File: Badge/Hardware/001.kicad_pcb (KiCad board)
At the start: 2 copper layers, 92.2 x 84.2 mm, 1 part

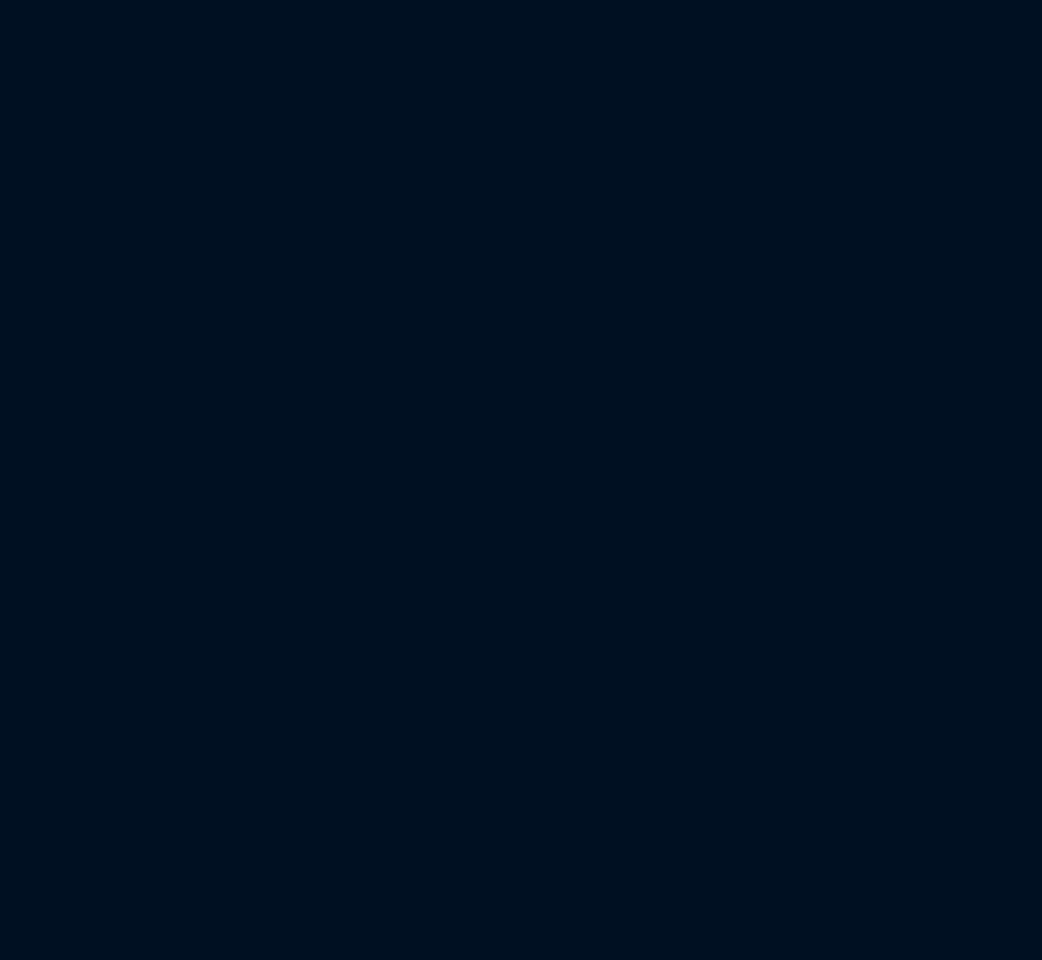
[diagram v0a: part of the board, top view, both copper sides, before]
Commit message: Add custom forms at SVG
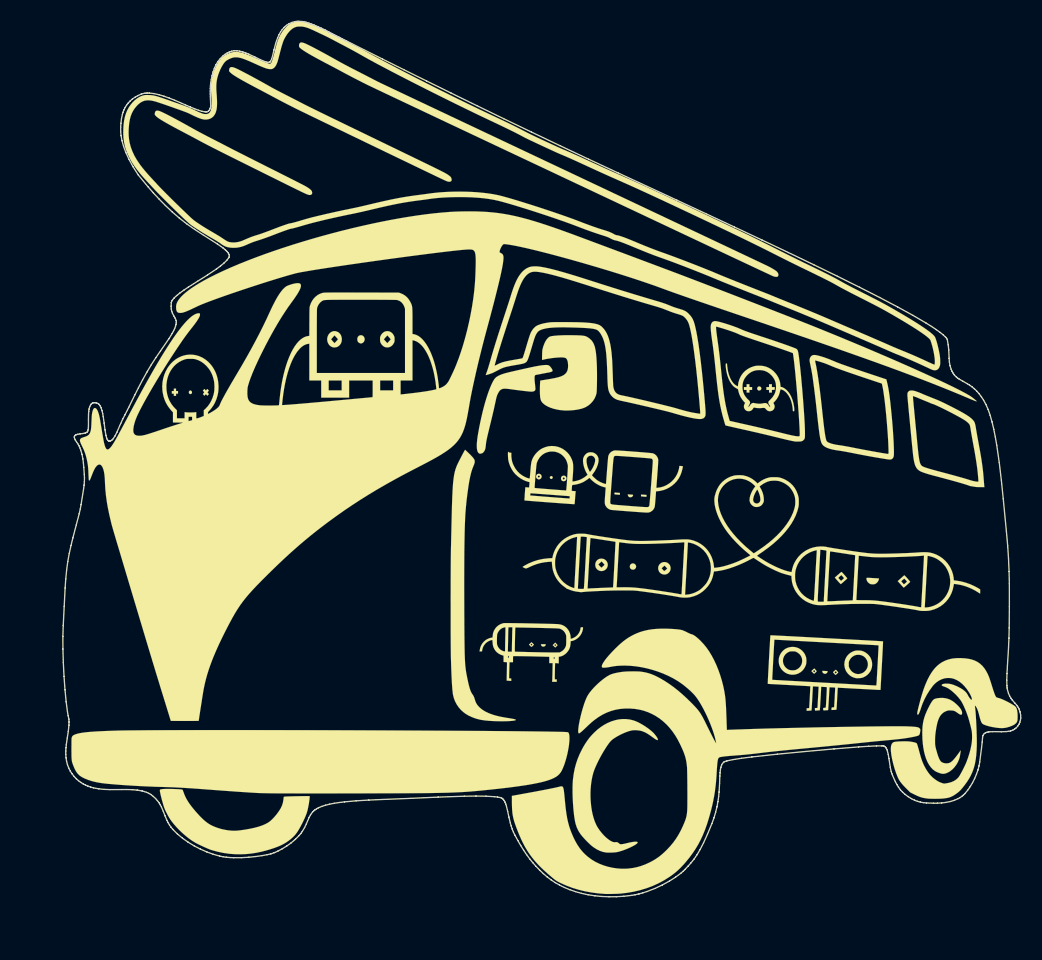
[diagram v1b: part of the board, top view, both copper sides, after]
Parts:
- added Ref**: Val**, combi:Combi_All_04, F.Cu at (232.4, 91.4)
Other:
- board size 92.2 x 84.2 mm -> 92.2 x 84.3 mm

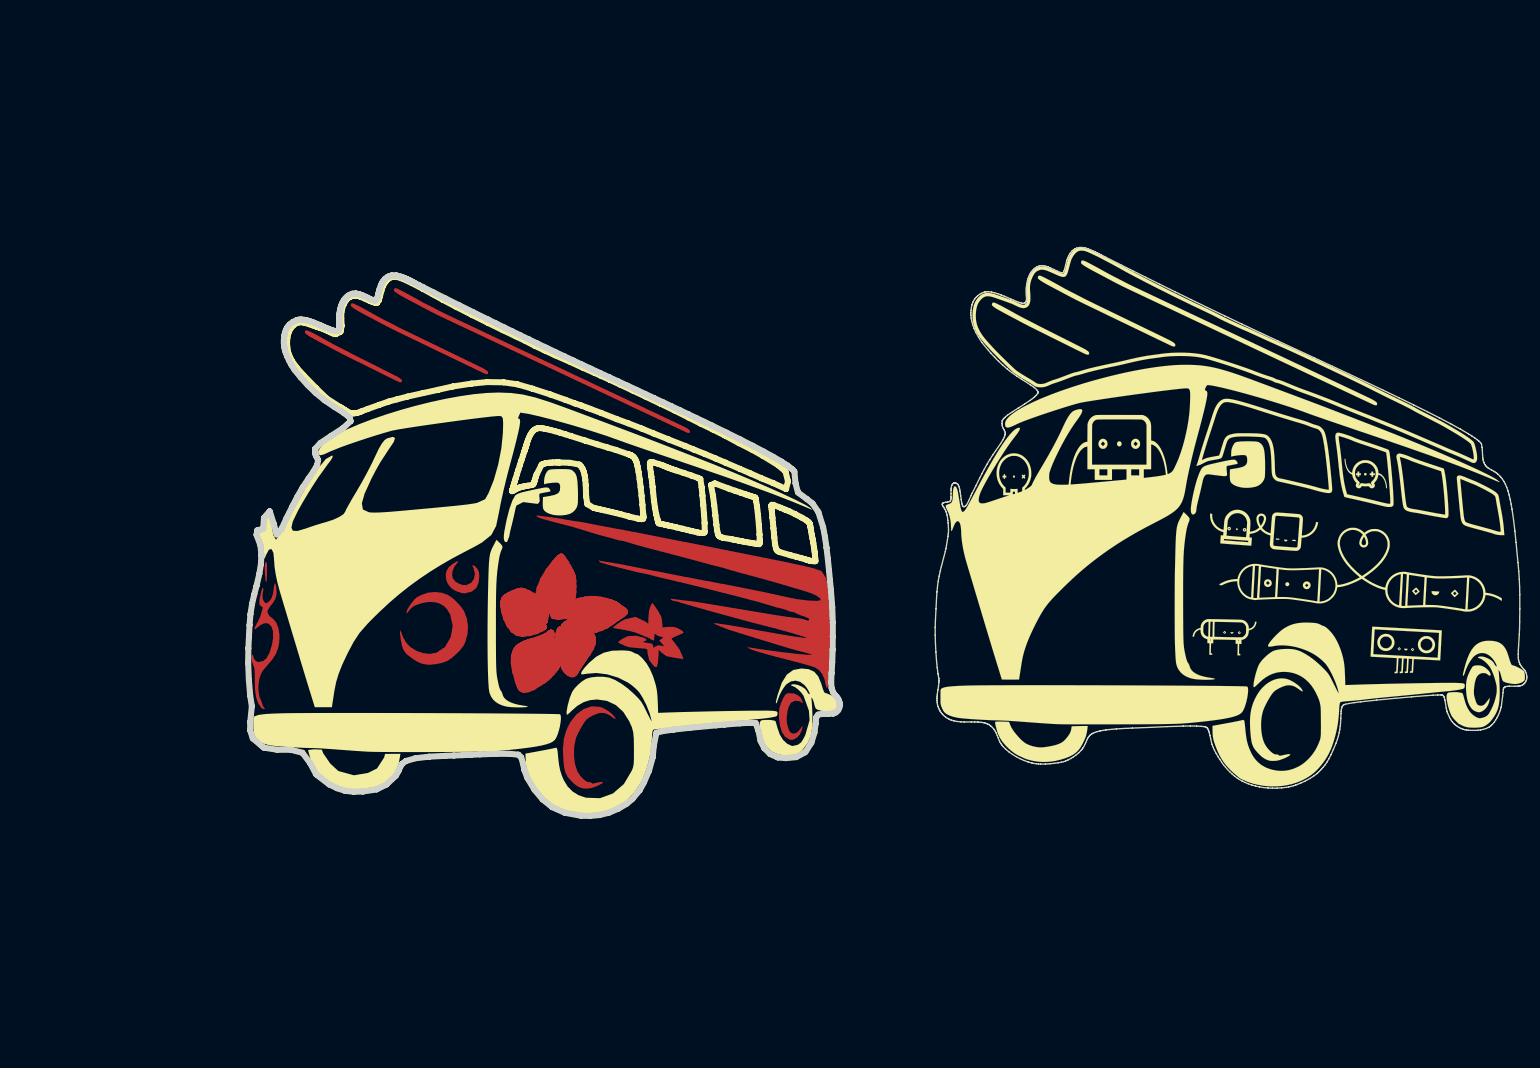
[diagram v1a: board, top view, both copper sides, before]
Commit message: Add custom art to SVG
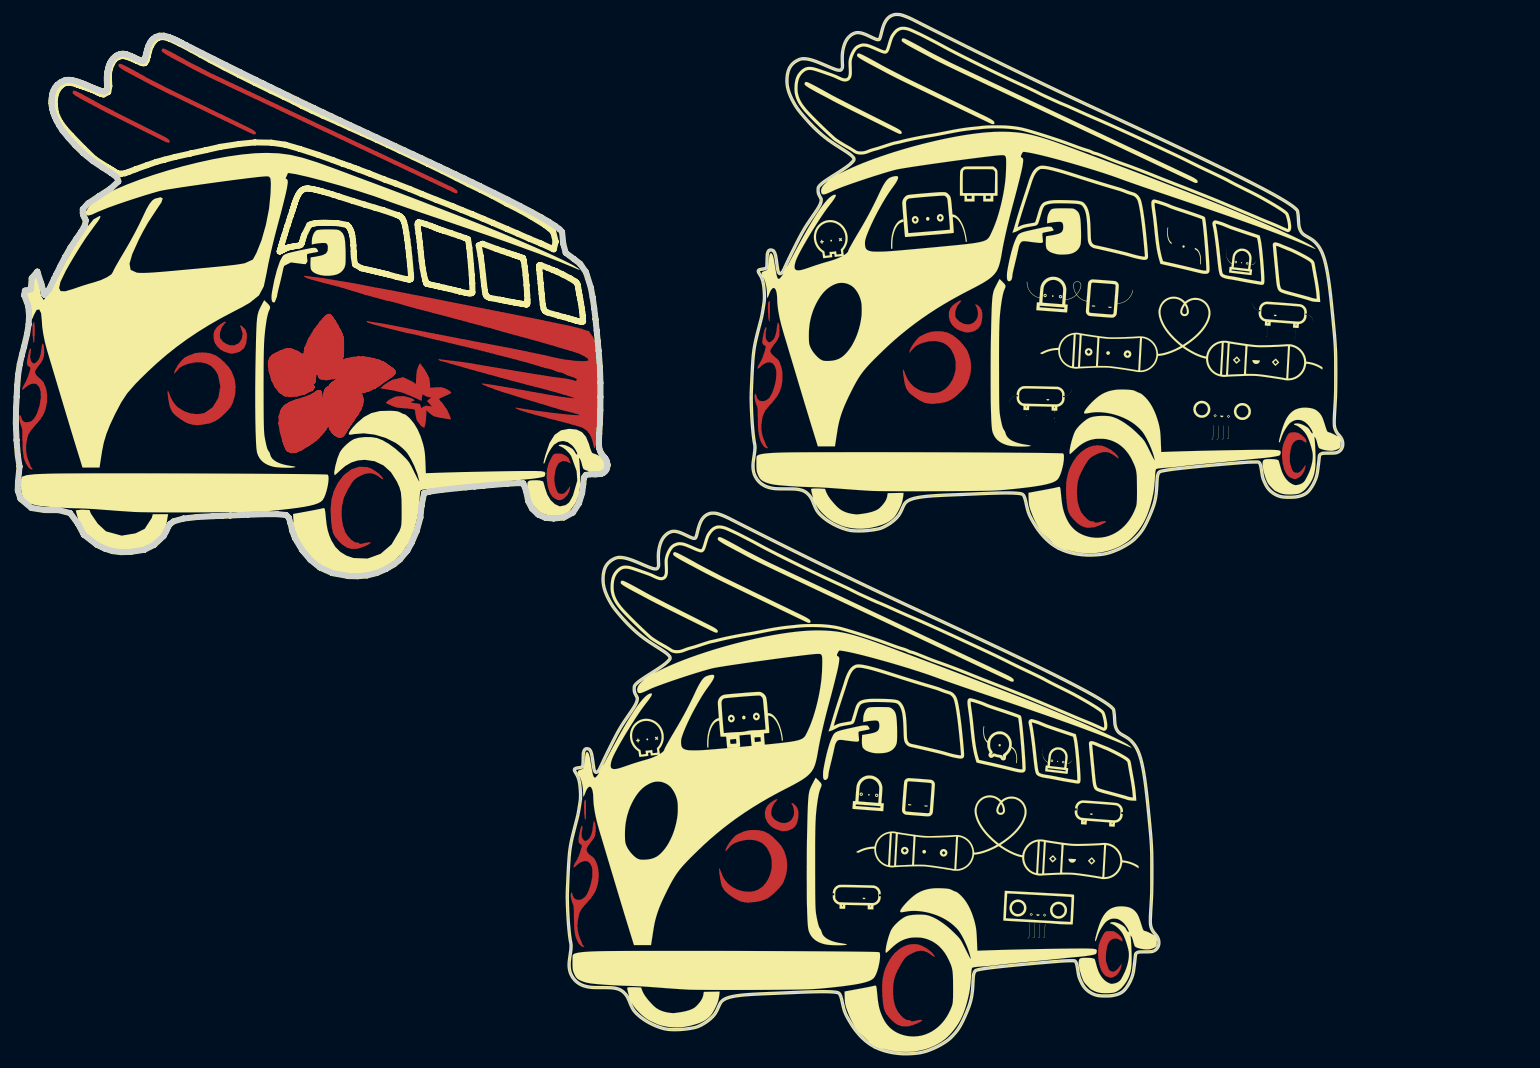
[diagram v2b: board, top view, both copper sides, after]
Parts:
- removed the Ref** at (232.4, 91.4)
- added Ref**: Val**, combi:Combi_06, F.Cu at (175.1, 132.8)
- added Ref**: Val**, combi:Combi_05, F.Cu at (203.7, 55.1)
- moved svg2mod 52.0 mm to (88.3, 58.5)

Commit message: Updates
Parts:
- removed the Ref** at (203.7, 55.1)
- removed svg2mod: G***, combi:Combi.All.03
- added Ref**: Val**, combi:logo_AGS_2022, F.Cu at (172.7, 118.1)
- moved Ref** 50.7 mm to (141.0, 95.2)

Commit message: Update Combi 4
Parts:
- removed the Ref** at (141.0, 95.2)
- added Ref**: Val**, combi:Combi_4, F.Cu at (147.3, 94.0)
- moved Ref** 7.86 mm to (180.3, 116.2)
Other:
- outline, holes or cut-outs redrawn

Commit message: Clear old files
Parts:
- moved Ref** 0.87 mm to (148.1, 94.4)
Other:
- outline, holes or cut-outs redrawn
